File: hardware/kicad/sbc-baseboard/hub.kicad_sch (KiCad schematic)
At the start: 84 parts, among them J1 USB-C upstream, J4 USB-A PORT1, J5 USB-A PORT3, U401 USBLC6-2SC6, U402 USB2517, U403 TPS2553DBV, U404 TPS2553DBV, U405 TPS2553DBV, U406 TPS2553DBV, U407 TPS2553DBV, U408 USBLC6-2SC6, U409 USBLC6-2SC6, U410 USBLC6-2SC6, U411 USBLC6-2SC6, Y401 24MHz

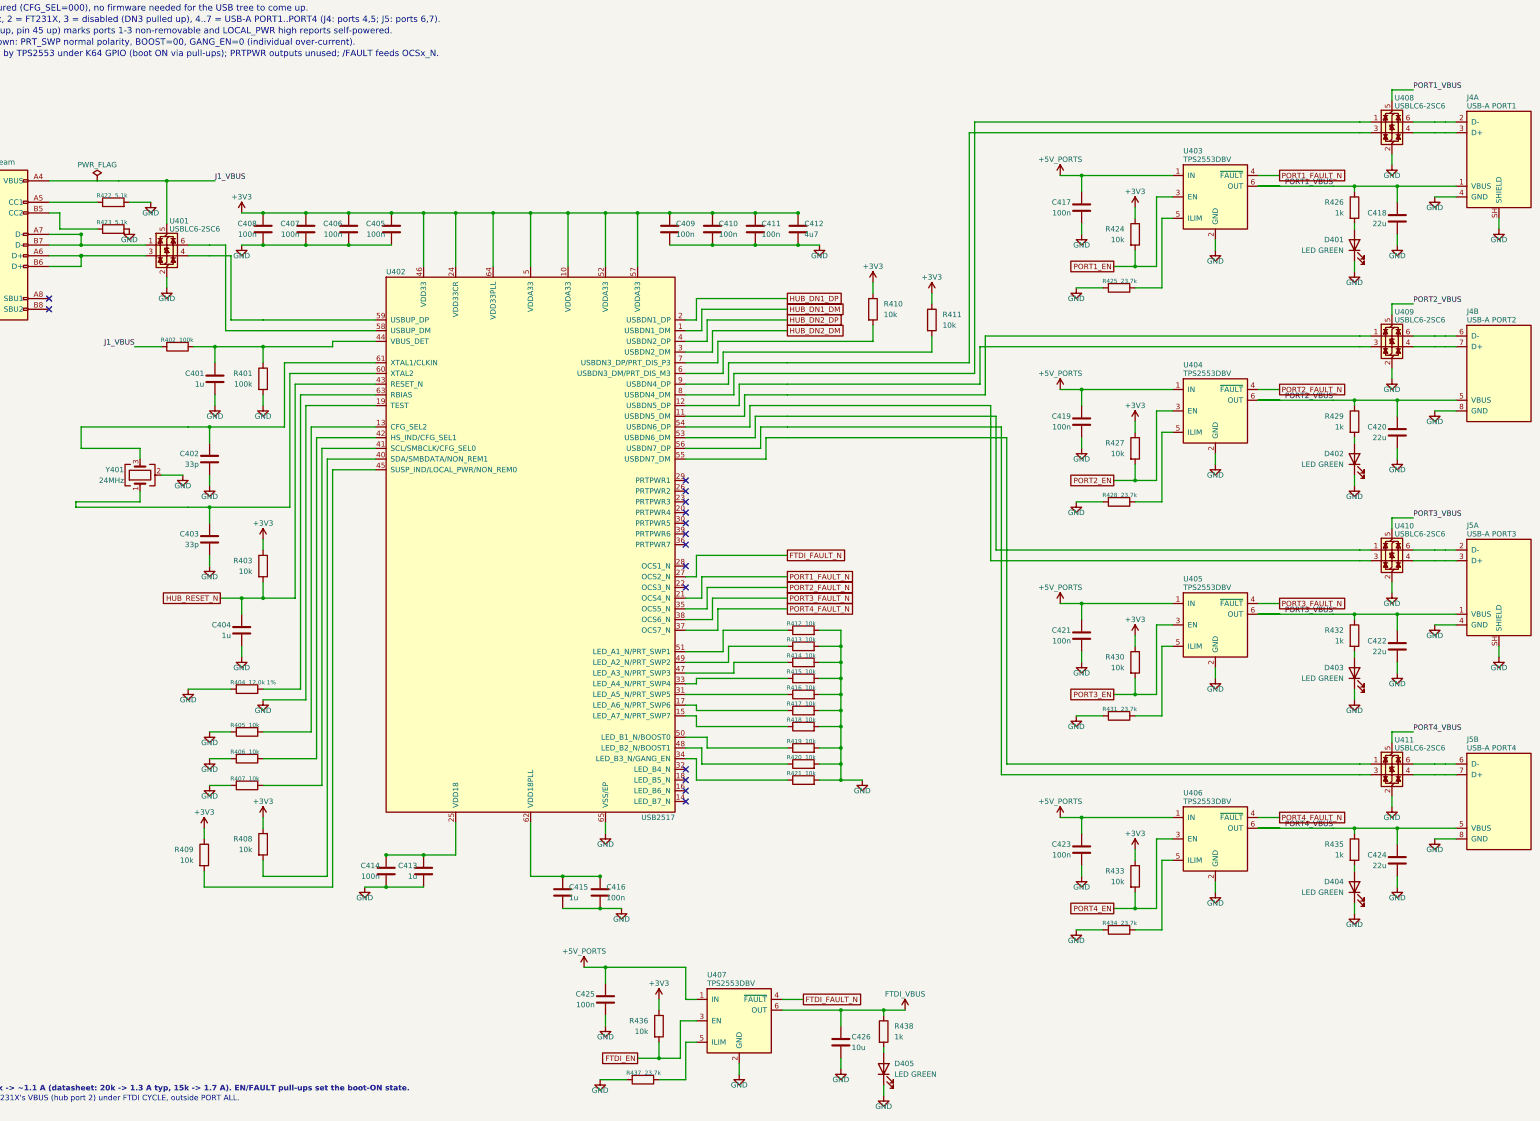
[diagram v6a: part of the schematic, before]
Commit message: House symbols from the ecad-libraries submodule
The project symbols move to calicopizzadelivery/ecad-libraries, added as a
submodule at hardware/kicad/libs and pinned to v0.1.1. The generator loads
them from the submodule's files (kisym.EXTRA_LIBS), so the embedded copies
match the library exactly; sym-lib-table and fp-lib-table are the fragments
the library ships, naming calico-ic and calico-electromechanical as
${KIPRJMOD}/../libs/... gen/parts.py and the project .kicad_sym are gone.

The symbols now follow the KiCad Library Conventions (every pin on the 100 mil
grid of the origin, 20 mil name offset), which moved a few pin rows; the port
blocks are re-aligned to the stacked USB-A's new rows. All sheets: ERC 0,
contacts 0, merges 0, layout 0; connectivity unchanged.

Co-Authored-By: Claude Fable 5.1 <noreply@anthropic.com>
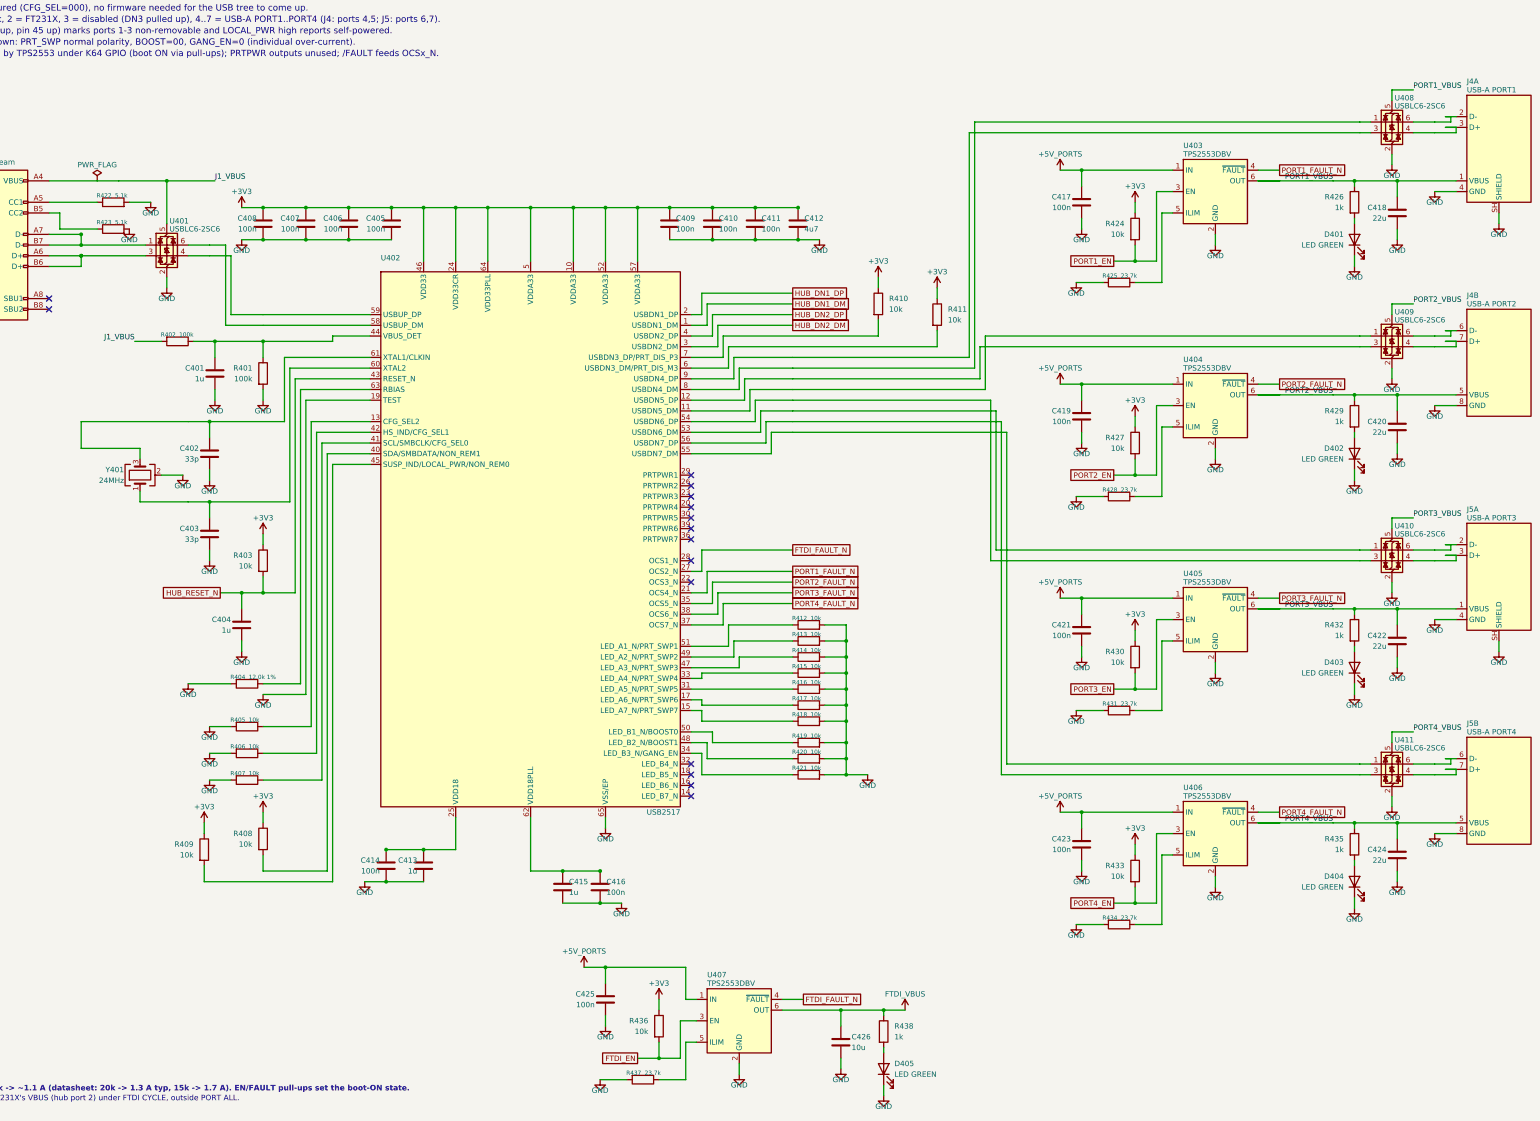
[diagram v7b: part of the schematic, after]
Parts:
- removed J4: USB-A PORT1, Connector_USB:USB_A_Wuerth_61400826021_Horizontal_Stacked, symbol sbcbb:USB_A_Stacked2
- removed J5: USB-A PORT4, Connector_USB:USB_A_Wuerth_61400826021_Horizontal_Stacked, symbol sbcbb:USB_A_Stacked2
- removed U402: USB2517, Package_DFN_QFN:QFN-64-1EP_9x9mm_P0.5mm_EP7.15x7.15mm, symbol sbcbb:USB2517
- removed U403, U404, U405, U406, U407: TPS2553DBV, Package_TO_SOT_SMD:SOT-23-6, symbol sbcbb:TPS2553DBV
- added J4: USB-A PORT1, Connector_USB:USB_A_Wuerth_61400826021_Horizontal_Stacked, symbol calico-electromechanical:USB_A_Stacked2
- added J5: USB-A PORT3, Connector_USB:USB_A_Wuerth_61400826021_Horizontal_Stacked, symbol calico-electromechanical:USB_A_Stacked2
- added U402: USB2517, Package_DFN_QFN:QFN-64-1EP_9x9mm_P0.5mm_EP7.15x7.15mm, symbol calico-ic:USB2517
- added U403, U404, U405, U406, U407: TPS2553DBV, Package_TO_SOT_SMD:SOT-23-6, symbol calico-ic:TPS2553DBV
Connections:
- net +3V3: now also U402.10 (VDDA33), U402.24 (VDD33CR), U402.46 (VDD33), U402.5 (VDDA33), U402.52 (VDDA33), U402.57 (VDDA33), U402.64 (VDD33PLL)
- net +5V_PORTS: now also U403.1 (IN), U404.1 (IN), U405.1 (IN), U406.1 (IN), U407.1 (IN)
- net FTDI_EN: now also U407.3 (EN)
- net FTDI_FAULT_N: now also U402.27 (OCS2_N), U407.4 (~{FAULT})
- net FTDI_VBUS: now also U407.6 (OUT)
- net GND: now also J4.4 (GND), J4.8 (GND), J4.SH (SHIELD), J5.4 (GND), J5.8 (GND), J5.SH (SHIELD), U402.19 (TEST), U402.65 (VSS/EP), U403.2 (GND), U404.2 (GND), U405.2 (GND), U406.2 (GND), U407.2 (GND)
- net HUB_DN1_DM: now also U402.1 (USBDN1_DM)
- net HUB_DN1_DP: now also U402.2 (USBDN1_DP)
- net HUB_DN2_DM: now also U402.3 (USBDN2_DM)
- net HUB_DN2_DP: now also U402.4 (USBDN2_DP)
- net HUB_RESET_N: now also U402.43 (RESET_N)
- net PORT1_EN: now also U403.3 (EN)
- net PORT1_FAULT_N: now also U402.21 (OCS4_N), U403.4 (~{FAULT})
- net PORT1_VBUS: now also J4.1 (VBUS), U403.6 (OUT)
- net PORT2_EN: now also U404.3 (EN)
- net PORT2_FAULT_N: now also U402.35 (OCS5_N), U404.4 (~{FAULT})
- net PORT2_VBUS: now also J4.5 (VBUS), U404.6 (OUT)
- net PORT3_EN: now also U405.3 (EN)
- net PORT3_FAULT_N: now also U402.38 (OCS6_N), U405.4 (~{FAULT})
- net PORT3_VBUS: now also J5.1 (VBUS), U405.6 (OUT)
- net PORT4_EN: now also U406.3 (EN)
- net PORT4_FAULT_N: now also U402.37 (OCS7_N), U406.4 (~{FAULT})
- net PORT4_VBUS: now also J5.5 (VBUS), U406.6 (OUT)
- net at R409.2: now also U402.45 (SUSP_IND/LOCAL_PWR/NON_REM0)
- net at C402.1, Y401.3: now also U402.61 (XTAL1/CLKIN)
- net at U411.1 (I/O1): now also U402.55 (USBDN7_DM)
- net at U411.3 (I/O2): now also U402.56 (USBDN7_DP)
- net at U411.4 (I/O2): now also J5.7 (D+)
- net at U411.6 (I/O1): now also J5.6 (D-)
- net at R407.1: now also U402.41 (SCL/SMBCLK/CFG_SEL0)
- net at R404.1: now also U402.63 (RBIAS)
- net at U408.6 (I/O1): now also J4.2 (D-)
- net at U408.4 (I/O2): now also J4.3 (D+)
- net at R437.1: now also U407.5 (ILIM)
- net at R428.1: now also U404.5 (ILIM)
- net at R421.1: now also U402.34 (LED_B3_N/GANG_EN)
- net at R420.1: now also U402.48 (LED_B2_N/BOOST1)
- net at R431.1: now also U405.5 (ILIM)
- net at R412.1: now also U402.51 (LED_A1_N/PRT_SWP1)
- net at R434.1: now also U406.5 (ILIM)
- net at R411.2: now also U402.6 (USBDN3_DM/PRT_DIS_M3)
- net at C415.1, C416.1: now also U402.62 (VDD18PLL)
- net at R425.1: now also U403.5 (ILIM)
- net at R410.2: now also U402.7 (USBDN3_DP/PRT_DIS_P3)
- net at C401.1, R401.1, R402.1: now also U402.44 (VBUS_DET)
- net at U409.1 (I/O1): now also U402.11 (USBDN5_DM)
- net at U409.3 (I/O2): now also U402.12 (USBDN5_DP)
- net at R405.1: now also U402.13 (CFG_SEL2)
- net at R418.1: now also U402.15 (LED_A7_N/PRT_SWP7)
- net at R417.1: now also U402.17 (LED_A6_N/PRT_SWP6)
- net at C413.1, C414.1: now also U402.25 (VDD18)
- net at R416.1: now also U402.31 (LED_A5_N/PRT_SWP5)
- net at R415.1: now also U402.33 (LED_A4_N/PRT_SWP4)
- net at R408.2: now also U402.40 (SDA/SMBDATA/NON_REM1)
- net at R406.1: now also U402.42 (HS_IND/CFG_SEL1)
- net at R414.1: now also U402.47 (LED_A3_N/PRT_SWP3)
- net at R413.1: now also U402.49 (LED_A2_N/PRT_SWP2)
- net at R419.1: now also U402.50 (LED_B1_N/BOOST0)
- net at U410.1 (I/O1): now also U402.53 (USBDN6_DM)
- net at U410.3 (I/O2): now also U402.54 (USBDN6_DP)
- net at U401.6 (I/O1): now also U402.58 (USBUP_DM)
- net at U401.4 (I/O2): now also U402.59 (USBUP_DP)
- net at C403.1, Y401.1: now also U402.60 (XTAL2)
- net at U408.1 (I/O1): now also U402.8 (USBDN4_DM)
- net at U408.3 (I/O2): now also U402.9 (USBDN4_DP)
- net at U410.4 (I/O2): now also J5.3 (D+)
- net at U410.6 (I/O1): now also J5.2 (D-)
- net at U409.4 (I/O2): now also J4.7 (D+)
- net at U409.6 (I/O1): now also J4.6 (D-)

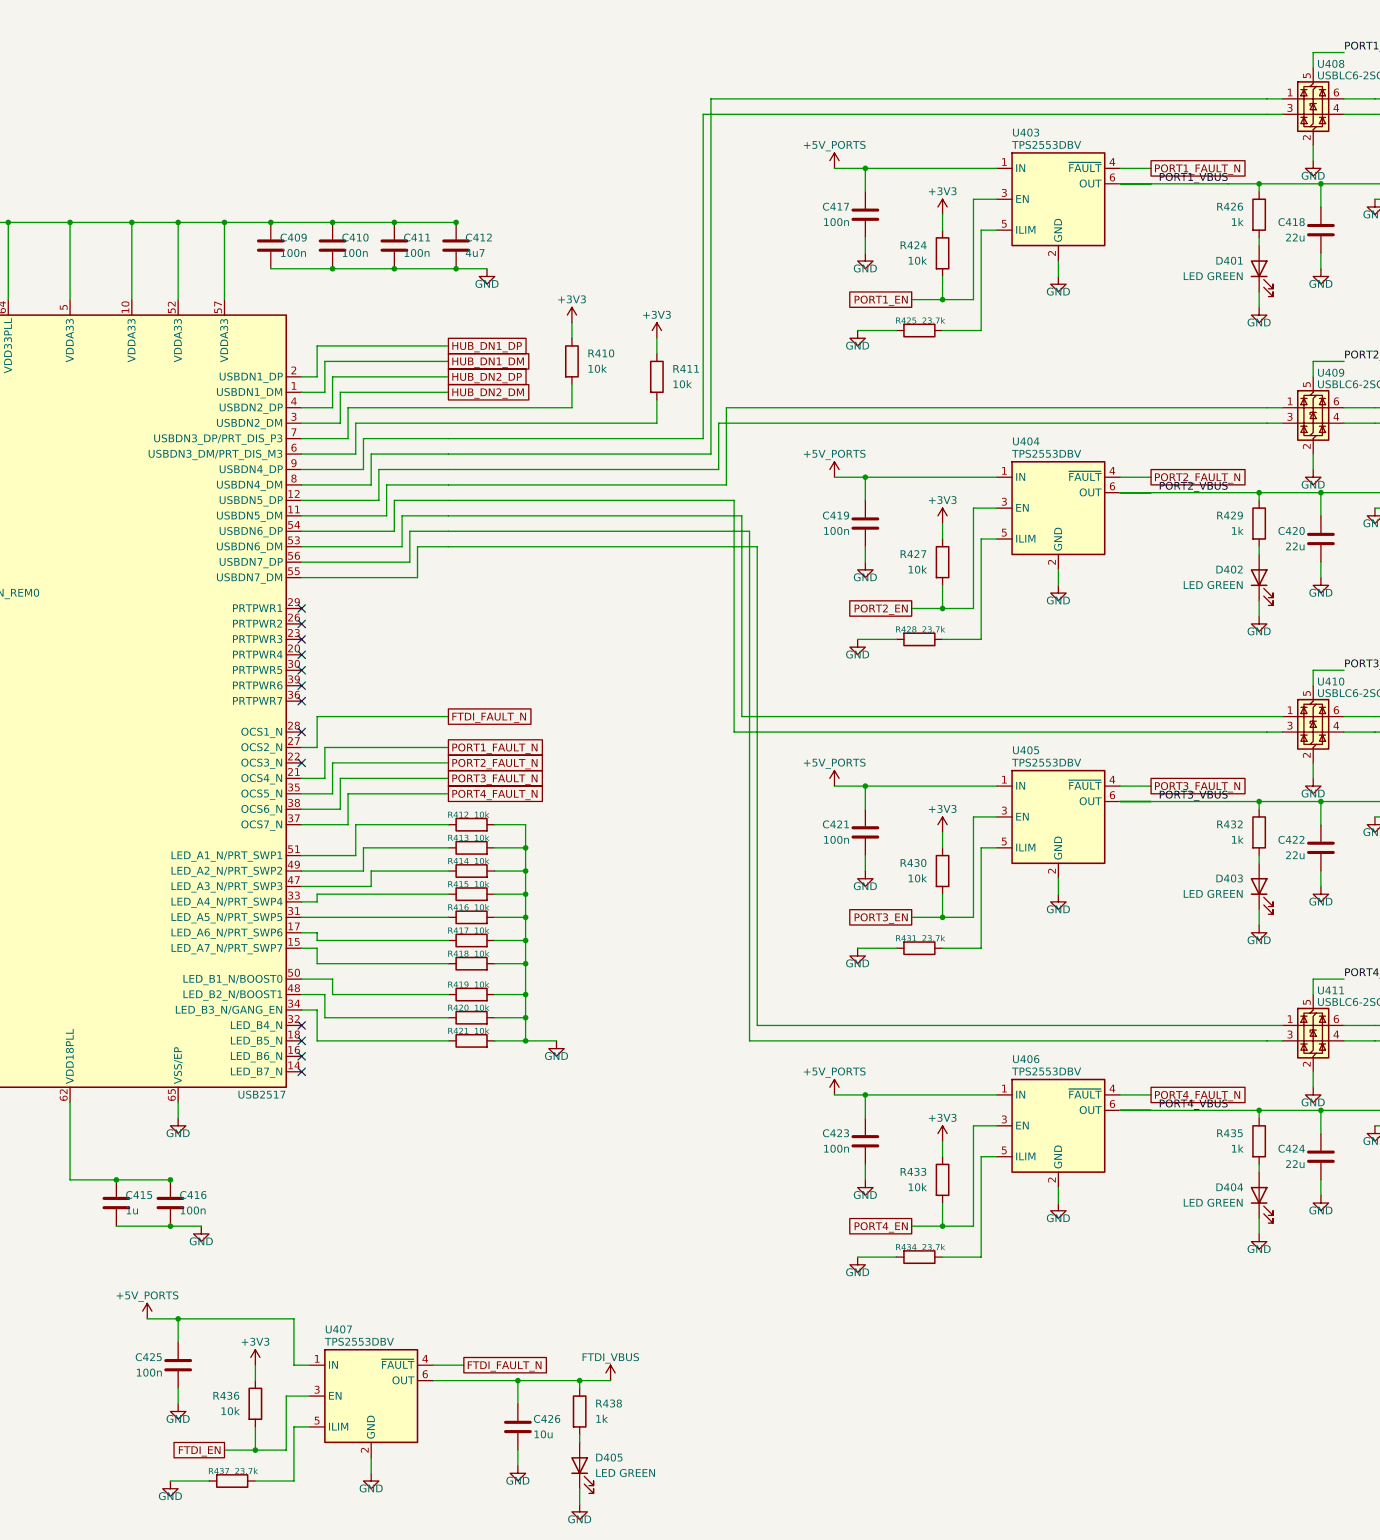
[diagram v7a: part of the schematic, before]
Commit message: Library v0.1.2; local-label text modelled above its wire
The port switch symbol gained a gap row between FAULT and OUT (ecad-libraries
v0.1.2): a local label's text prints above its wire, which the layout gate
had modelled as centred on it, so the switched-rail label and the FAULT
label printed over each other unreported. The gate now places a local
label's box 0.3 to 2.0 mm above the anchor, measured on KiCad's render;
U407 moves up for its new OUT row. All sheets clean on every gate.

Co-Authored-By: Claude Fable 5.1 <noreply@anthropic.com>
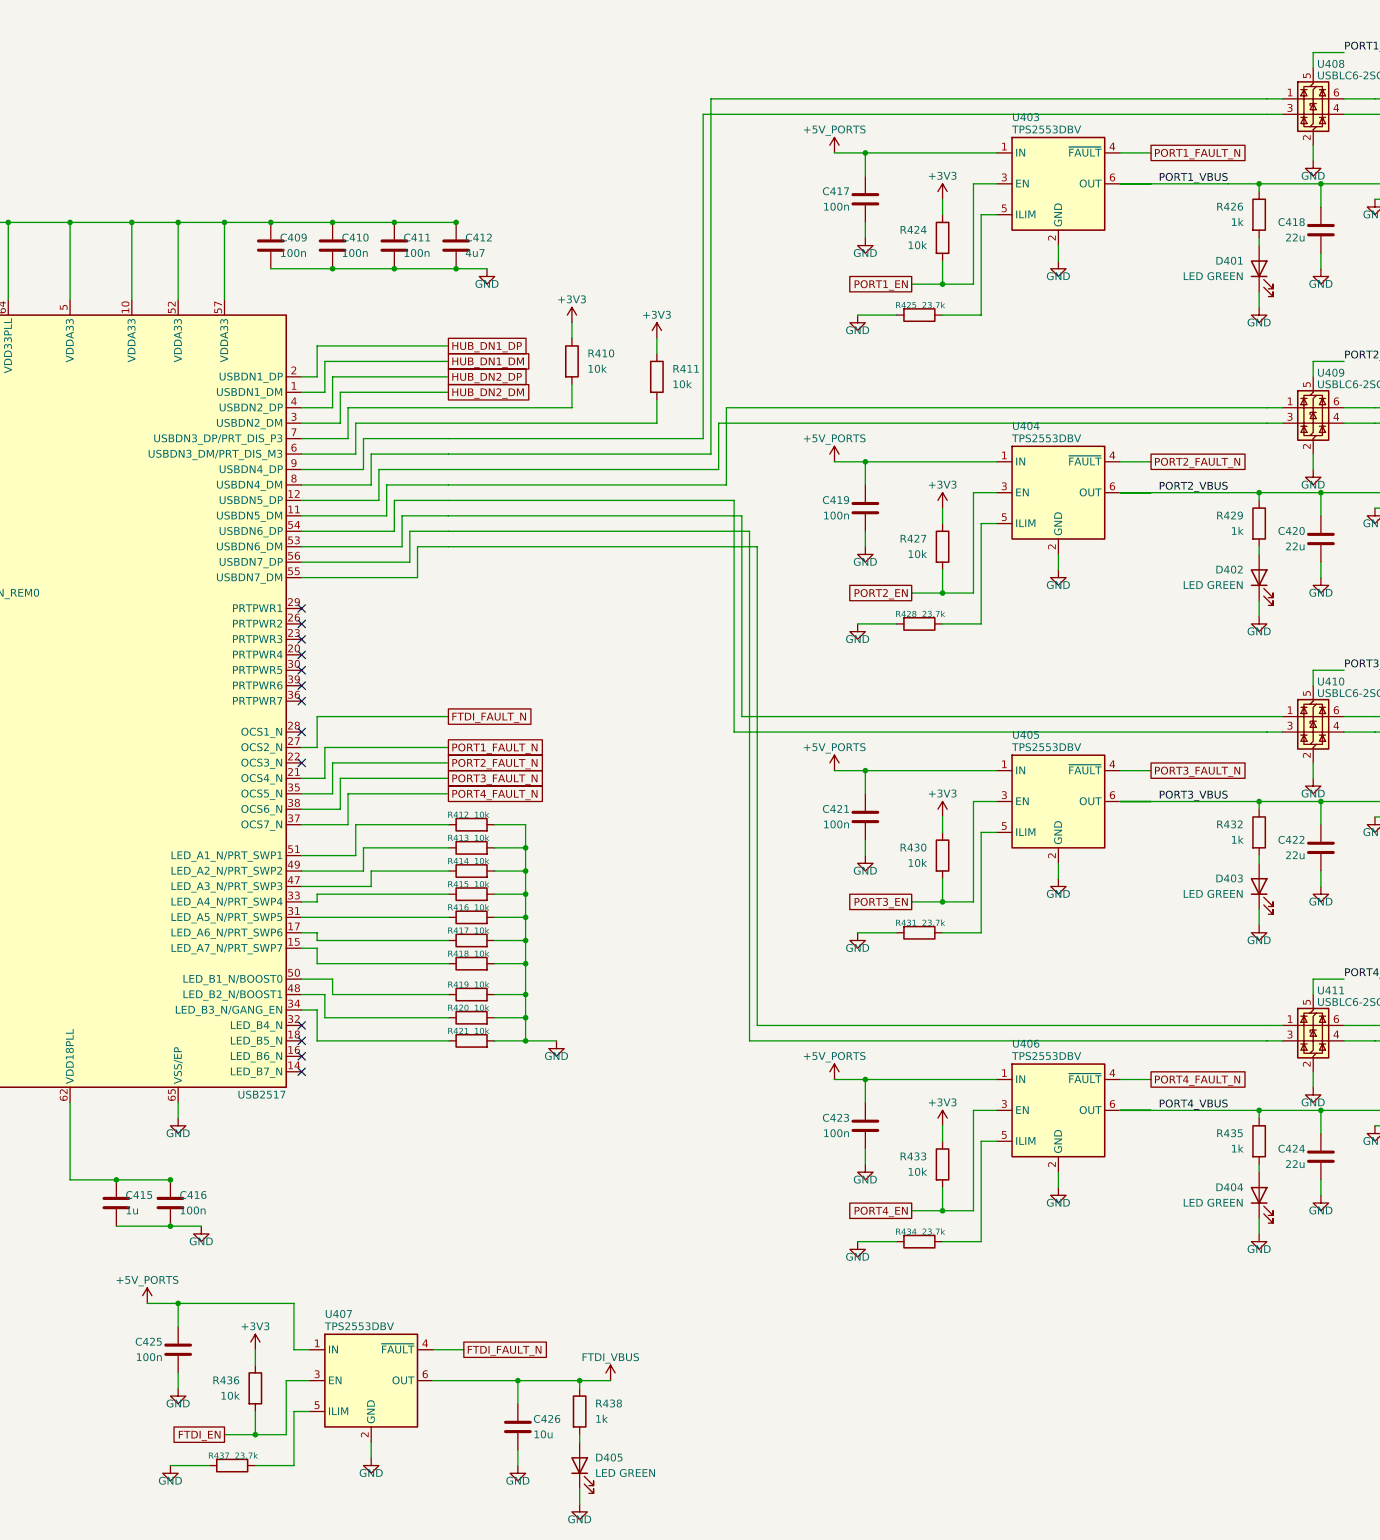
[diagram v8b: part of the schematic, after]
